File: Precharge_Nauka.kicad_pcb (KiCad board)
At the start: 4 copper layers, 100.8 x 98.4 mm, 246 parts, among them J1 Conn_02x03_Top_Bottom, J2 Conn_01x01, J3 Conn_01x01, J4 Conn_01x01, Q1 2N7002, Q2 C2M0280120D, Q3 C2M0280120D, Q4 C2M0280120D, Q5 C2M0280120D, Q6 2N7002, U1 TS3702IDT, U3 74LVC1G08, U5 PC817, U6 OPA333xxDBV, U7 OPA333xxDBV

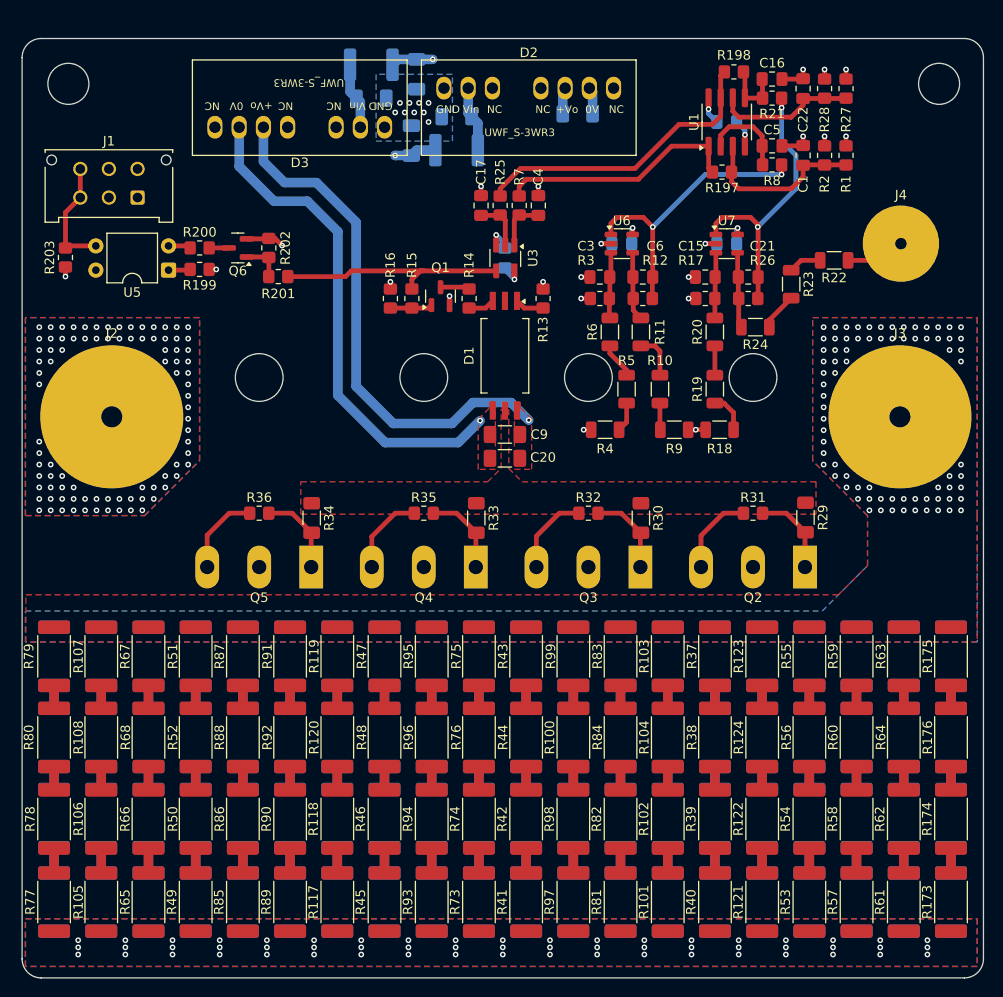
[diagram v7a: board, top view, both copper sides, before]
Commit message: VER1.0: подготовил файлы для производства v1.0
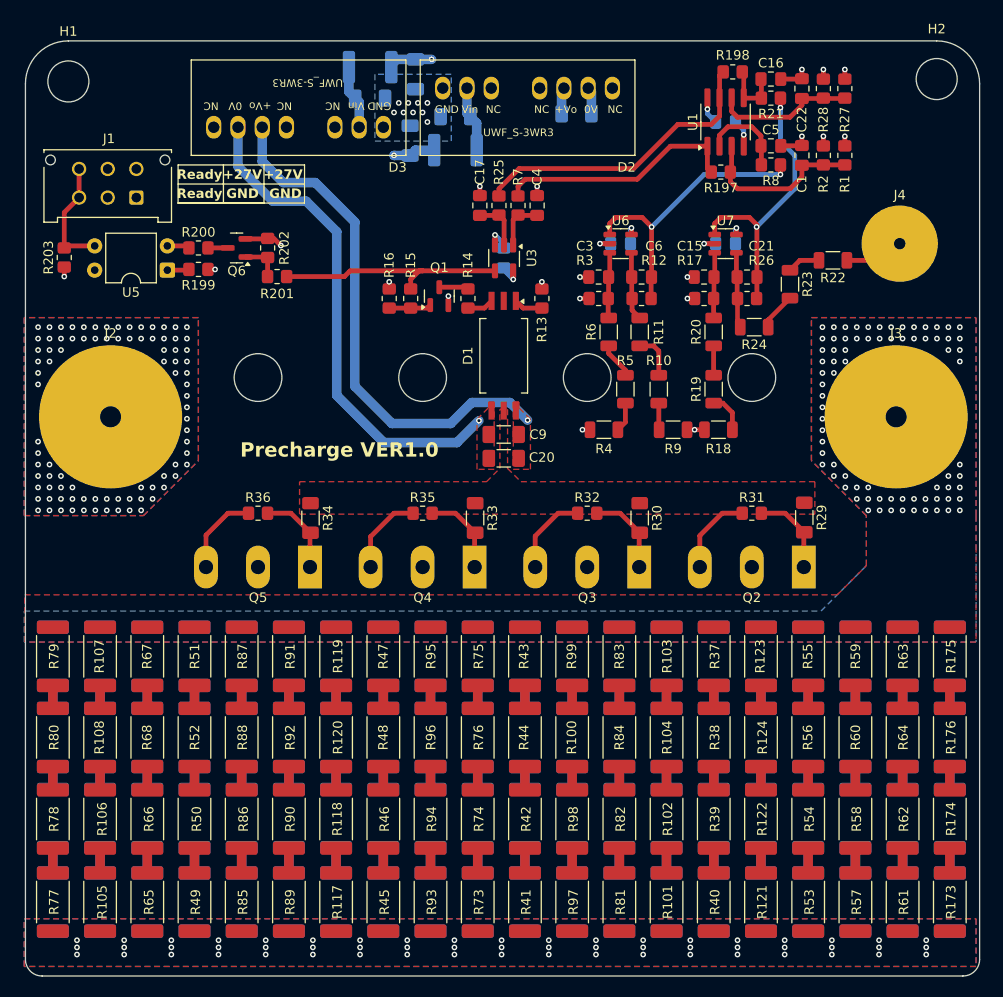
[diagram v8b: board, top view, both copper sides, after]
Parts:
- D1: value NSI6801 -> ~
- D2: value UWF1205S-3WR3 -> ~
- D3: value UWF1215S-3WR3 -> ~
- H1, H2: value MountingHole -> ~
- J1: value Conn_02x03_Top_Bottom -> ~
- J2, J3, J4: value Conn_01x01 -> ~
- Q1, Q6: value 2N7002 -> ~
- Q2, Q3, Q4, Q5: value C2M0280120D -> ~
- U1: value TS3702IDT -> ~
- U3: value 74LVC1G08 -> ~
- U5: value PC817 -> ~
- U6, U7: value OPA333xxDBV -> ~
- moved H2 0.56 mm to (231.2, 129.0)
- moved J3 0.40 mm to (227.0, 164.4)
- moved L2 0.28 mm to (171.9, 127.8)
- moved H1 0.25 mm to (140.2, 129.2)
- moved C1 0.12 mm to (217.1, 137.0)
- moved C10 0.12 mm to (209.1, 133.5)
- moved C11 0.12 mm to (176.1, 135.4)
- moved C12 0.12 mm to (180.8, 132.9)
- moved C13 0.12 mm to (193.5, 132.6)
- moved C14 0.12 mm to (209.1, 146.2)
- moved C15 0.12 mm to (206.9, 149.8)
- moved C16 0.12 mm to (213.9, 129.0)
- moved C17 0.12 mm to (183.4, 142.2)
- moved C18 0.12 mm to (176.6, 128.5)
- moved C19 0.12 mm to (171.9, 131.0)
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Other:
- board size 100.8 x 98.4 mm -> 100 x 98 mm
- board text added: "+27V"
- board text added: "GND"
- board text added: "Precharge VER1.0"
- board text added: "Ready"
